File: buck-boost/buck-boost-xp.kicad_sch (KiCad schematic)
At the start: 14 parts, among them J1 Conn_02x08_Odd_Even, J10 Conn_01x01, J2 Conn_02x08_Odd_Even, J3 Conn_01x01, J4 Conn_01x01, J5 Conn_01x01, J6 Conn_01x01, J7 Conn_01x01, J8 Conn_01x01, J9 Conn_01x01

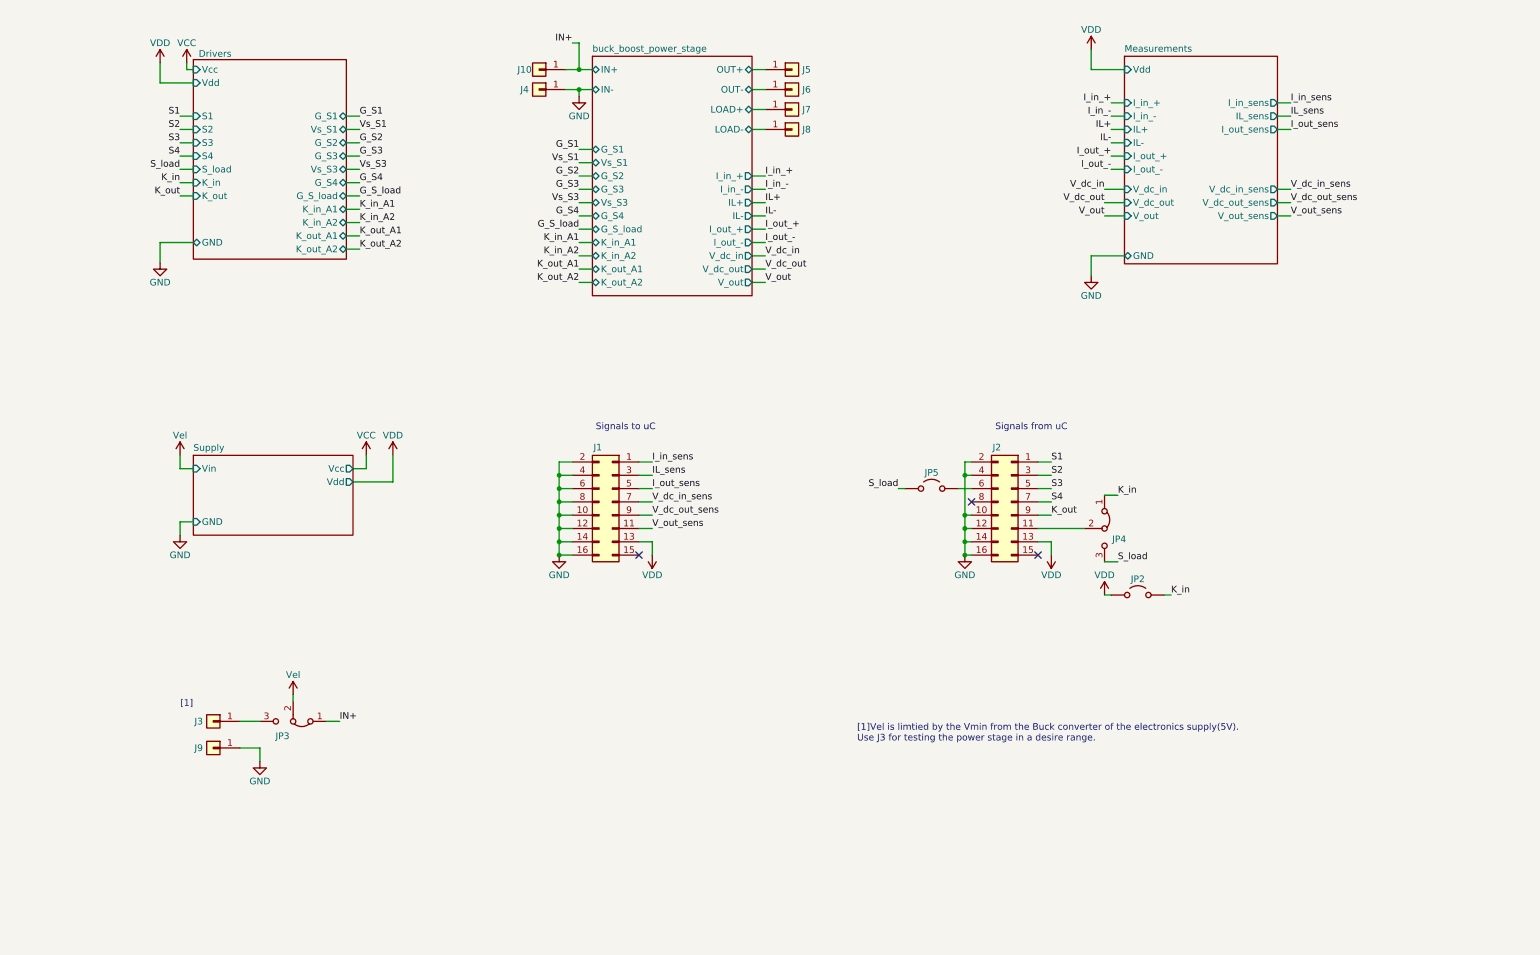
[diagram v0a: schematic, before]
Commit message: The changes indicated in the text document Review. 05.11.2024 were implemented. Missing footprints were added
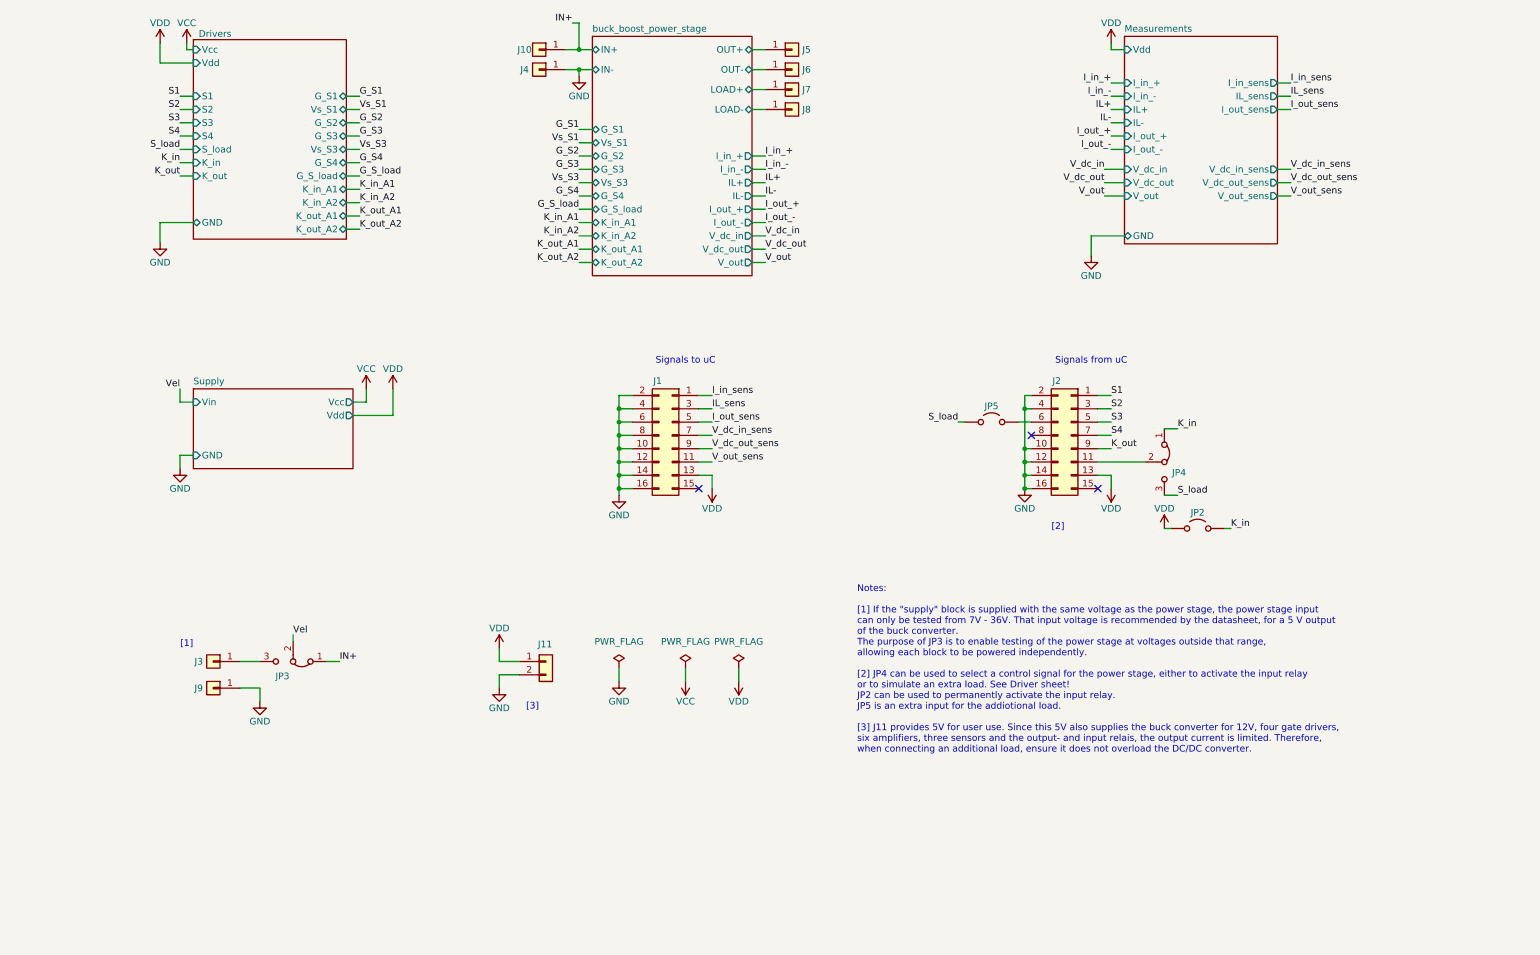
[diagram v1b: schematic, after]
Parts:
- added J11: Conn_01x02, Connector_PinHeader_2.54mm:PinHeader_1x02_P2.54mm_Vertical, symbol Connector_Generic:Conn_01x02
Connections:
- net GND: now also J11.2 (Pin_2)
- net VDD: now also J11.1 (Pin_1)
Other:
- sheet Supply: file buck-boost.kicad_sch -> Supply.kicad_sch
- note added: "Notes: [1] If the "supply" block is supplied with the same voltage as the power stage, the power stage input can only be tested from 7V - 36V. That input voltage is recommended by the datasheet, for a 5 V output of the buck converter. The purpose of JP3 is to enable testing of the power stage at voltages outside that range, allowing each block to be powered independently. [2] JP4 can be used to s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"
- note added: "[2]"
- note added: "[3]"
- note removed: "[1]Vel is limtied by the Vmin from the Buck converter of the electronics supply(5V). Use J3 for testing the power stage in a desire range."
- moved on the sheet: J1, J10, J2, J3, J4, J5, J6, J7, J8, J9, JP2, JP3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

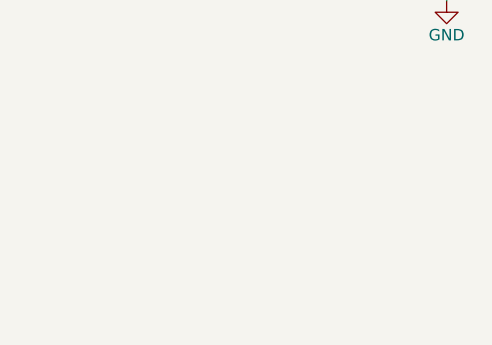
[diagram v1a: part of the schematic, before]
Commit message: Some errors in the schematics were corrected. PCB file V1.0
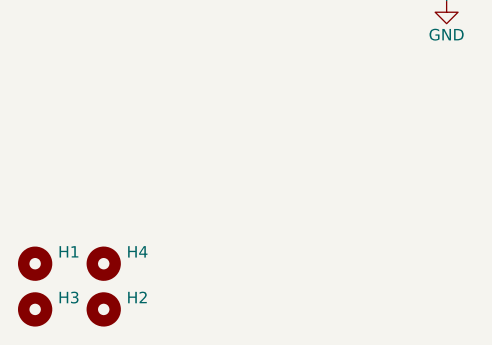
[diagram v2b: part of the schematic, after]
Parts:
- added H1, H2, H3, H4: MountingHole, MountingHole:MountingHole_3.2mm_M3, symbol Mechanical:MountingHole

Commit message: Update V1.0
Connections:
- net IL_sens: now also J1.5 (Pin_5); no longer J1.3 (Pin_3)
- net I_out_sens: now also J1.9 (Pin_9); no longer J1.5 (Pin_5)
- net V_dc_in_sens: now also J1.3 (Pin_3); no longer J1.7 (Pin_7)
- net V_dc_out_sens: now also J1.11 (Pin_11); no longer J1.9 (Pin_9)
- net V_out_sens: now also J1.7 (Pin_7); no longer J1.11 (Pin_11)
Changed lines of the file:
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@@
 	)
 	(label "V_dc_in_sens"
-		(at 149.86 97.79 0)
+		(at 149.86 92.71 0)
 		(fields_autoplaced yes)
 		(effects
@@
 	)
 	(label "V_out_sens"
-		(at 149.86 102.87 0)
+		(at 149.86 97.79 0)
 		(fields_autoplaced yes)
 		(effects
@@
 	)
 	(label "V_dc_out_sens"
-		(at 149.86 100.33 0)
+		(at 149.86 102.87 0)
 		(fields_autoplaced yes)
 		(effects
@@
 	)
 	(label "IL_sens"
-		(at 149.86 92.71 0)
+		(at 149.86 95.25 0)
 		(fields_autoplaced yes)
 		(effects
@@
 	)
 	(label "I_out_sens"
-		(at 149.86 95.25 0)
-		(fields_autoplaced yes)
-		(effects
+		(at 149.86 100.33 0)
+		(fields_autoplaced yes)
+		(effects

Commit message: V1.0 finished. Teardrops were added.
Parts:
- added H5, H6: MountingHole, MountingHole:MountingHole_3.2mm_M3, symbol Mechanical:MountingHole
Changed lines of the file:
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@@
+	)
+	(symbol
+		(lib_name "MountingHole_3")
+		(lib_id "Mechanical:MountingHole")
+		(at 17.78 187.96 0)
+		(unit 1)
+		(exclude_from_sim yes)
+		(in_bom no)
+		(on_board yes)
+		(dnp no)
+		(fields_autoplaced yes)
+		(property "Reference" "H5"
+			(at 20.32 186.6899 0)
+			(effects
+				(font
+					(size 1.27 1.27)
+				)
+				(justify left)
+			)
+		)
+		(property "Value" "MountingHole"
+			(at 20.32 189.2299 0)
+			(effects
+				(font
+					(size 1.27 1.27)
+				)
+				(justify left)
+				(hide yes)
+			)
+		)
+		(property "Footprint" "MountingHole:MountingHole_3.2mm_M3"
+			(at 17.78 187.96 0)
+			(effects
+				(font
+					(size 1.27 1.27)
+				)
+				(hide yes)
+			)
+		)
+		(property "Datasheet" "~"
+			(at 17.78 187.96 0)
+			(effects
+				(font
+					(size 1.27 1.27)
+				)
+				(hide yes)
+			)
+		)
+		(property "Description" "Mounting Hole without connection"
+			(at 17.78 187.96 0)
+			(effects
+				(font
+					(size 1.27 1.27)
+				)
+				(hide yes)
+			)
+		)
+		(instances
+			(project "buck-boost-xp"
+				(path "/3f994017-d36f-4c43-a8c8-740bd919e8ad"
+					(reference "H5")
+					(unit 1)
+				)
+			)
+		)
 	)
 	(symbol
@@
 					(unit 1)
 				)
+			)
+		)
+	)
+	(symbol
+		(lib_name "MountingHole_2")
+		(lib_id "Mechanical:MountingHole")
+		(at 25.4 187.96 0)
+		(unit 1)
+		(exclude_from_sim yes)
+		(in_bom no)
+		(on_board yes)
+		(dnp no)
+		(fields_autoplaced yes)
+		(property "Reference" "H6"
+			(at 27.94 186.6899 0)
+			(effects
+				(font
+					(size 1.27 1.27)
+				)
+				(justify left)
+			)
+		)
+		(property "Value" "MountingHole"
+			(at 27.94 189.2299 0)
+			(effects
+				(font
+					(size 1.27 1.27)
+				)
+				(justify left)
+				(hide yes)
+			)
+		)
+		(property "Footprint" "MountingHole:MountingHole_3.2mm_M3"
+			(at 25.4 187.96 0)
+			(effects
+				(font
+					(size 1.27 1.27)
+				)
+				(hide yes)
+			)
+		)
+		(property "Datasheet" "~"
+			(at 25.4 187.96 0)
+			(effects
+				(font
+					(size 1.27 1.27)
+				)
+				(hide yes)
+			)
+		)
+		(property "Description" "Mounting Hole without connection"
+			(at 25.4 187.96 0)
+			(effects
+				(font
+					(size 1.27 1.27)
+				)
+				(hide yes)
+			)
+		)
+		(instances
+			(project "buck-boost-xp"
+				(path "/3f994017-d36f-4c43-a8c8-740bd919e8ad"
+					(reference "H6")
+					(unit 1)
+				)

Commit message: V1.1. Changes regarding to Review 16.12.2024
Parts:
- added H7: MountingHole, MountingHole:MountingHole_3.2mm_M3, symbol Mechanical:MountingHole
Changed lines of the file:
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@@
+	)
+	(symbol
+		(lib_name "MountingHole_2")
+		(lib_id "Mechanical:MountingHole")
+		(at 17.78 193.04 0)
+		(unit 1)
+		(exclude_from_sim yes)
+		(in_bom no)
+		(on_board yes)
+		(dnp no)
+		(fields_autoplaced yes)
+		(property "Reference" "H7"
+			(at 20.32 191.7699 0)
+			(effects
+				(font
+					(size 1.27 1.27)
+				)
+				(justify left)
+			)
+		)
+		(property "Value" "MountingHole"
+			(at 20.32 194.3099 0)
+			(effects
+				(font
+					(size 1.27 1.27)
+				)
+				(justify left)
+				(hide yes)
+			)
+		)
+		(property "Footprint" "MountingHole:MountingHole_3.2mm_M3"
+			(at 17.78 193.04 0)
+			(effects
+				(font
+					(size 1.27 1.27)
+				)
+				(hide yes)
+			)
+		)
+		(property "Datasheet" "~"
+			(at 17.78 193.04 0)
+			(effects
+				(font
+					(size 1.27 1.27)
+				)
+				(hide yes)
+			)
+		)
+		(property "Description" "Mounting Hole without connection"
+			(at 17.78 193.04 0)
+			(effects
+				(font
+					(size 1.27 1.27)
+				)
+				(hide yes)
+			)
+		)
+		(instances
+			(project "buck-boost-xp"
+				(path "/3f994017-d36f-4c43-a8c8-740bd919e8ad"
+					(reference "H7")
+					(unit 1)
+				)
+			)
+		)
 	)
 	(symbol
